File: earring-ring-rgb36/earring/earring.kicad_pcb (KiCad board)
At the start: 4 copper layers, 25 x 27.3 mm, 44 parts, among them J1 Conn_01x04, SW1 SW_Push, U2 STM32L031G6Ux

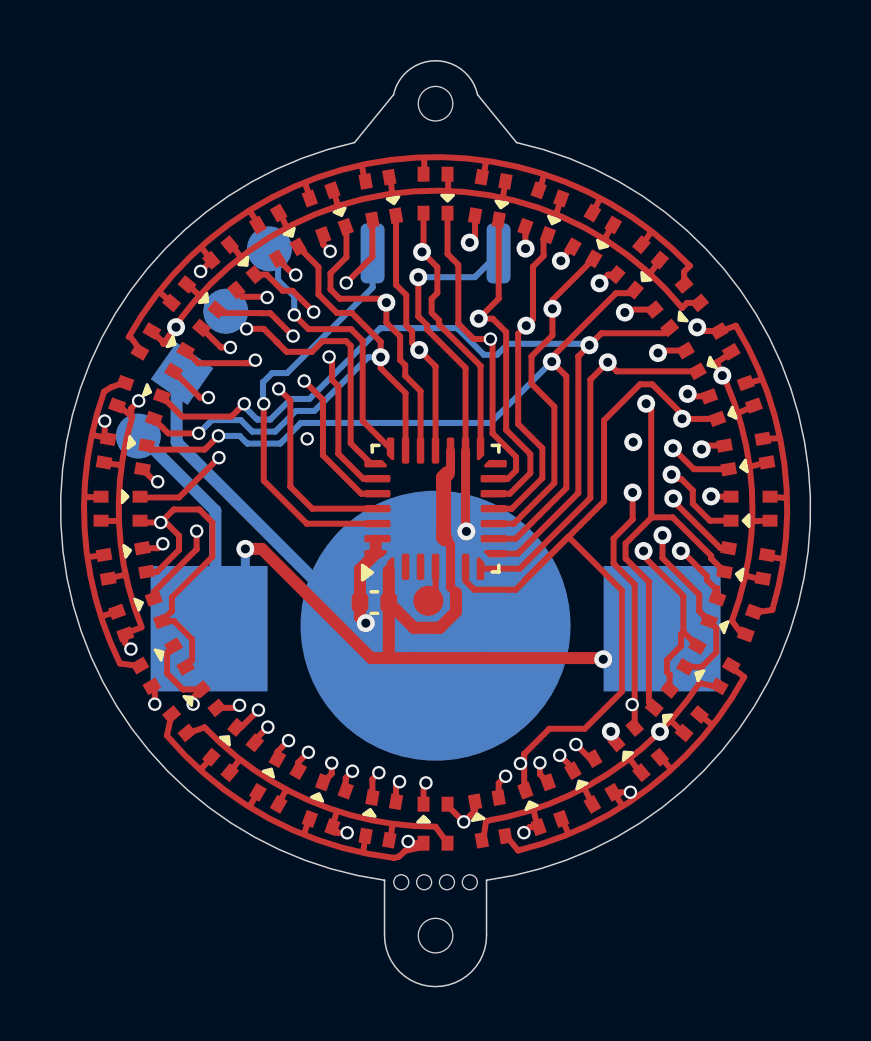
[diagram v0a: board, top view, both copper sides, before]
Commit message: earring-ring-rgb36: completely redid the schematic/PCB
Use 9x4 instead of 6x6 rows of LEDs. This should be more efficient to
control in software and actually simplifies the PCB a lot.

I also redid the routing of the PCB entirely:

  * Sit closer to the JLCPCB trace distance limit. Now most traces are
    0.2mm wide with 0.1mm spacing, whereas the limit is 0.10mm/0.10mm.
  * Put *two* traces between the LEDs. This simplifies the layout
    massively.
  * Switch to a two-layer board. We don't need the middle layers
    anymore with the above simplifications. This should make things
    cheaper and offer more options regarding color etc.
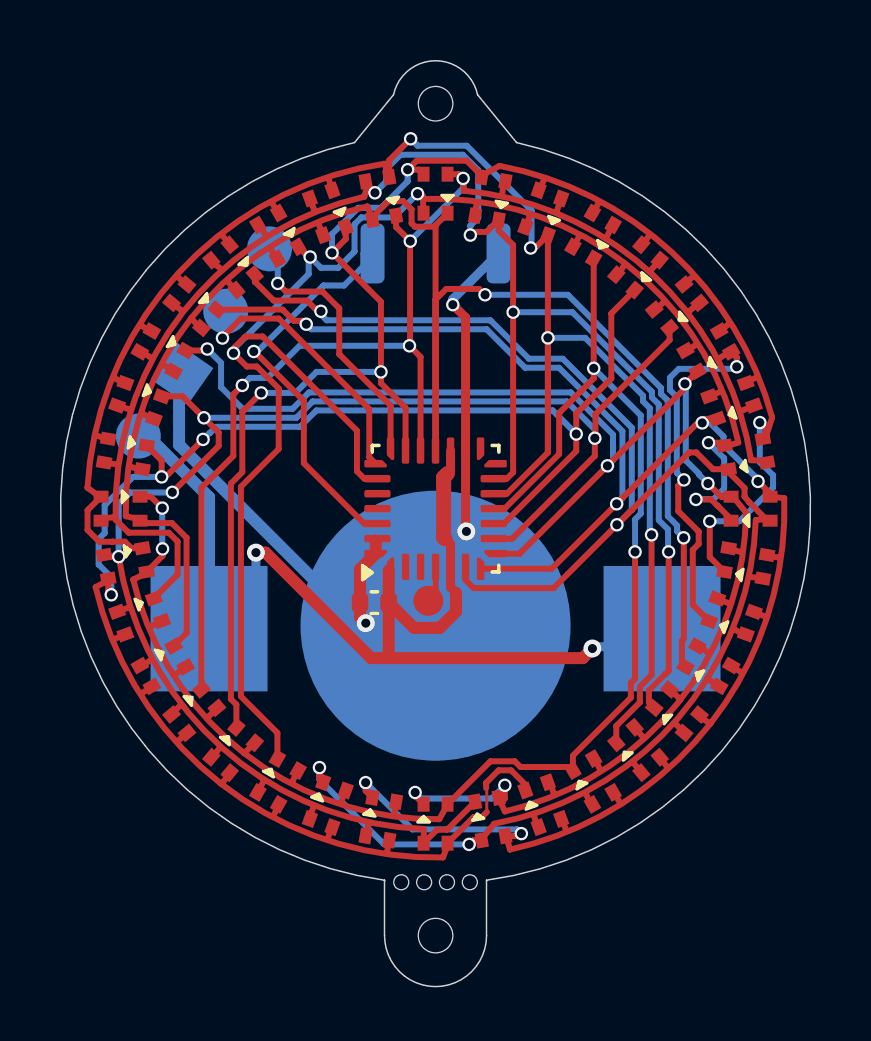
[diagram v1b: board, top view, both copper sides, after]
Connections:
- D1 pad 2: R1 -> A10
- D1 pad 3: G1 -> A11
- D1 pad 4: B1 -> A12
- D10 pad 2: A1 -> A7
- D10 pad 3: A2 -> A8
- D10 pad 4: A3 -> A9
- D11 pad 2: A1 -> A7
- D11 pad 3: A2 -> A8
- D11 pad 4: A3 -> A9
- D12 pad 2: A1 -> A7
- D12 pad 3: A2 -> A8
- D12 pad 4: A3 -> A9
- D13 pad 1: A12 -> A1
- D13 pad 2: A4 -> A7
- D13 pad 3: A5 -> A8
- D13 pad 4: A6 -> A9
- D14 pad 1: A11 -> A2
- D14 pad 2: A4 -> A7
- D14 pad 3: A5 -> A8
- D14 pad 4: A6 -> A9
- D15 pad 1: A10 -> A3
- D15 pad 2: A4 -> A7
- D15 pad 3: A5 -> A8
- D15 pad 4: A6 -> A9
- D16 pad 1: A9 -> A4
- D16 pad 2: A4 -> A7
- D16 pad 3: A5 -> A8
- D16 pad 4: A6 -> A9
- D17 pad 1: A8 -> A5
- D17 pad 2: A4 -> A7
- D17 pad 3: A5 -> A8
- D17 pad 4: A6 -> A9
- D18 pad 1: A7 -> A6
- D18 pad 2: A4 -> A7
- D18 pad 3: A5 -> A8
- D18 pad 4: A6 -> A9
- D19 pad 1: A6 -> A7
- D19 pad 2: A7 -> A4
- D19 pad 3: A8 -> A5
- D19 pad 4: A9 -> A6
- D2 pad 2: R1 -> A10
- D2 pad 3: G1 -> A11
- D2 pad 4: B1 -> A12
- D20 pad 1: A5 -> A8
- D20 pad 2: A7 -> A4
- D20 pad 3: A8 -> A5
- D20 pad 4: A9 -> A6
- D21 pad 1: A4 -> A9
- D21 pad 2: A7 -> A4
- D21 pad 3: A8 -> A5
- D21 pad 4: A9 -> A6
- D22 pad 1: A3 -> A10
- D22 pad 2: A7 -> A4
- D22 pad 3: A8 -> A5
- D22 pad 4: A9 -> A6
- D23 pad 1: A2 -> A11
- D23 pad 2: A7 -> A4
- D23 pad 3: A8 -> A5
- D23 pad 4: A9 -> A6
- D24 pad 1: A1 -> A12
- D24 pad 2: A7 -> A4
- D24 pad 3: A8 -> A5
- D24 pad 4: A9 -> A6
- D25 pad 2: A10 -> A4
- D25 pad 3: A11 -> A5
- D25 pad 4: A12 -> A6
- D26 pad 2: A10 -> A4
- D26 pad 3: A11 -> A5
- D26 pad 4: A12 -> A6
- D27 pad 2: A10 -> A4
- D27 pad 3: A11 -> A5
- D27 pad 4: A12 -> A6
- D28 pad 2: A10 -> A1
- D28 pad 3: A11 -> A2
- D28 pad 4: A12 -> A3
- D29 pad 2: A10 -> A1
- D29 pad 3: A11 -> A2
- D29 pad 4: A12 -> A3
- D3 pad 2: R1 -> A10
- D3 pad 3: G1 -> A11
- D3 pad 4: B1 -> A12
- D30 pad 2: A10 -> A1
- D30 pad 3: A11 -> A2
- D30 pad 4: A12 -> A3
- D31 pad 2: R1 -> A1
- D31 pad 3: G1 -> A2
- D31 pad 4: B1 -> A3
- D32 pad 2: R1 -> A1
- D32 pad 3: G1 -> A2
- D32 pad 4: B1 -> A3
- D33 pad 2: R1 -> A1
- D33 pad 3: G1 -> A2
- D33 pad 4: B1 -> A3
- D34 pad 2: R1 -> A1
- D34 pad 3: G1 -> A2
- D34 pad 4: B1 -> A3
- D35 pad 2: R1 -> A1
- D35 pad 3: G1 -> A2
- D35 pad 4: B1 -> A3
- D36 pad 2: R1 -> A1
- D36 pad 3: G1 -> A2
- D36 pad 4: B1 -> A3
- D4 pad 2: R1 -> A10
- D4 pad 3: G1 -> A11
- D4 pad 4: B1 -> A12
- D5 pad 2: R1 -> A10
- D5 pad 3: G1 -> A11
- D5 pad 4: B1 -> A12
- D6 pad 2: R1 -> A10
- D6 pad 3: G1 -> A11
- D6 pad 4: B1 -> A12
- D7 pad 2: A1 -> A10
- D7 pad 3: A2 -> A11
- D7 pad 4: A3 -> A12
- D8 pad 2: A1 -> A10
- D8 pad 3: A2 -> A11
- D8 pad 4: A3 -> A12
- D9 pad 2: A1 -> A10
- D9 pad 3: A2 -> A11
- D9 pad 4: A3 -> A12
- U2 pad 10: A4 -> A5
- U2 pad 11: A3 -> A4
- U2 pad 12: A2 -> A3
- U2 pad 13: A1 -> A2
- U2 pad 15: R1 -> unconnected-(U2-PB1-Pad15)
- U2 pad 18: A12 -> A1
- U2 pad 19: A11 -> A12
- U2 pad 20: A10 -> A11
- U2 pad 23: A9 -> A10
- U2 pad 24: G1 -> unconnected-(U2-PB3-Pad24)
- U2 pad 25: B1 -> unconnected-(U2-PB6-Pad25)
- U2 pad 6: A8 -> A9
- U2 pad 7: A7 -> A8
- U2 pad 8: A6 -> A7
- U2 pad 9: A5 -> A6
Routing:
- net R1: track 40.4 -> 0.00 mm, vias 12 -> 0
- net A4: track 70.1 -> 33.1 mm, vias 9 -> 4
- net A10: track 55.3 -> 38.5 mm, vias 6 -> 5
- net A5: track 52.4 -> 36.9 mm
- net A7: track 51.2 -> 35.8 mm, vias 8 -> 6
- net A1: track 55.7 -> 40.5 mm, vias 8 -> 2
- net A8: track 52.7 -> 38.3 mm, vias 4 -> 6
- net G1: track 13.0 -> 0.00 mm, vias 2 -> 0
- net B1: track 12.5 -> 0.00 mm, vias 2 -> 0
- net A6: track 47.5 -> 35.3 mm, vias 5 -> 4
- net A9: track 49.6 -> 39.4 mm, vias 5 -> 4
- net A11: track 48.8 -> 39.6 mm, vias 5 -> 6
- net A2: track 44.1 -> 39.3 mm
- net A3: track 46.4 -> 41.6 mm, vias 5 -> 4
- net GND: track 28.8 -> 26.7 mm
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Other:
- copper layers 4 -> 2

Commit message: earring-ring-rgb36: rotate net names so the labels make a bit more sense
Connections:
- D1 pad 1: A1 -> A4
- D1 pad 2: A10 -> A1
- D1 pad 3: A11 -> A2
- D1 pad 4: A12 -> A3
- D10 pad 1: A10 -> A1
- D10 pad 2: A7 -> A10
- D10 pad 3: A8 -> A11
- D10 pad 4: A9 -> A12
- D11 pad 1: A11 -> A2
- D11 pad 2: A7 -> A10
- D11 pad 3: A8 -> A11
- D11 pad 4: A9 -> A12
- D12 pad 1: A12 -> A3
- D12 pad 2: A7 -> A10
- D12 pad 3: A8 -> A11
- D12 pad 4: A9 -> A12
- D13 pad 1: A1 -> A4
- D13 pad 2: A7 -> A10
- D13 pad 3: A8 -> A11
- D13 pad 4: A9 -> A12
- D14 pad 1: A2 -> A5
- D14 pad 2: A7 -> A10
- D14 pad 3: A8 -> A11
- D14 pad 4: A9 -> A12
- D15 pad 1: A3 -> A6
- D15 pad 2: A7 -> A10
- D15 pad 3: A8 -> A11
- D15 pad 4: A9 -> A12
- D16 pad 1: A4 -> A7
- D16 pad 2: A7 -> A10
- D16 pad 3: A8 -> A11
- D16 pad 4: A9 -> A12
- D17 pad 1: A5 -> A8
- D17 pad 2: A7 -> A10
- D17 pad 3: A8 -> A11
- D17 pad 4: A9 -> A12
- D18 pad 1: A6 -> A9
- D18 pad 2: A7 -> A10
- D18 pad 3: A8 -> A11
- D18 pad 4: A9 -> A12
- D19 pad 1: A7 -> A10
- D19 pad 2: A4 -> A7
- D19 pad 3: A5 -> A8
- D19 pad 4: A6 -> A9
- D2 pad 1: A2 -> A5
- D2 pad 2: A10 -> A1
- D2 pad 3: A11 -> A2
- D2 pad 4: A12 -> A3
- D20 pad 1: A8 -> A11
- D20 pad 2: A4 -> A7
- D20 pad 3: A5 -> A8
- D20 pad 4: A6 -> A9
- D21 pad 1: A9 -> A12
- D21 pad 2: A4 -> A7
- D21 pad 3: A5 -> A8
- D21 pad 4: A6 -> A9
- D22 pad 1: A10 -> A1
- D22 pad 2: A4 -> A7
- D22 pad 3: A5 -> A8
- D22 pad 4: A6 -> A9
- D23 pad 1: A11 -> A2
- D23 pad 2: A4 -> A7
- D23 pad 3: A5 -> A8
- D23 pad 4: A6 -> A9
- D24 pad 1: A12 -> A3
- D24 pad 2: A4 -> A7
- D24 pad 3: A5 -> A8
- D24 pad 4: A6 -> A9
- D25 pad 1: A1 -> A4
- D25 pad 2: A4 -> A7
- D25 pad 3: A5 -> A8
- D25 pad 4: A6 -> A9
- D26 pad 1: A2 -> A5
- D26 pad 2: A4 -> A7
- D26 pad 3: A5 -> A8
- D26 pad 4: A6 -> A9
- D27 pad 1: A3 -> A6
- D27 pad 2: A4 -> A7
- D27 pad 3: A5 -> A8
- D27 pad 4: A6 -> A9
- D28 pad 1: A4 -> A7
- D28 pad 2: A1 -> A4
- D28 pad 3: A2 -> A5
- D28 pad 4: A3 -> A6
- D29 pad 1: A5 -> A8
- D29 pad 2: A1 -> A4
- D29 pad 3: A2 -> A5
- D29 pad 4: A3 -> A6
- D3 pad 1: A3 -> A6
- D3 pad 2: A10 -> A1
- D3 pad 3: A11 -> A2
- D3 pad 4: A12 -> A3
- D30 pad 1: A6 -> A9
- D30 pad 2: A1 -> A4
- D30 pad 3: A2 -> A5
- D30 pad 4: A3 -> A6
- D31 pad 1: A7 -> A10
- D31 pad 2: A1 -> A4
- D31 pad 3: A2 -> A5
- D31 pad 4: A3 -> A6
- D32 pad 1: A8 -> A11
- D32 pad 2: A1 -> A4
- D32 pad 3: A2 -> A5
- D32 pad 4: A3 -> A6
- D33 pad 1: A9 -> A12
- D33 pad 2: A1 -> A4
- D33 pad 3: A2 -> A5
- D33 pad 4: A3 -> A6
- D34 pad 1: A10 -> A1
- D34 pad 2: A1 -> A4
- D34 pad 3: A2 -> A5
- D34 pad 4: A3 -> A6
- D35 pad 1: A11 -> A2
- D35 pad 2: A1 -> A4
- D35 pad 3: A2 -> A5
- D35 pad 4: A3 -> A6
- D36 pad 1: A12 -> A3
- D36 pad 2: A1 -> A4
- D36 pad 3: A2 -> A5
- D36 pad 4: A3 -> A6
- D4 pad 1: A4 -> A7
- D4 pad 2: A10 -> A1
- D4 pad 3: A11 -> A2
- D4 pad 4: A12 -> A3
- D5 pad 1: A5 -> A8
- D5 pad 2: A10 -> A1
- D5 pad 3: A11 -> A2
- D5 pad 4: A12 -> A3
- D6 pad 1: A6 -> A9
- D6 pad 2: A10 -> A1
- D6 pad 3: A11 -> A2
- D6 pad 4: A12 -> A3
- D7 pad 1: A7 -> A10
- D7 pad 2: A10 -> A1
- D7 pad 3: A11 -> A2
- D7 pad 4: A12 -> A3
- D8 pad 1: A8 -> A11
- D8 pad 2: A10 -> A1
- D8 pad 3: A11 -> A2
- D8 pad 4: A12 -> A3
- D9 pad 1: A9 -> A12
- D9 pad 2: A10 -> A1
- D9 pad 3: A11 -> A2
- D9 pad 4: A12 -> A3
- U2 pad 10: A5 -> A8
- U2 pad 11: A4 -> A7
- U2 pad 12: A3 -> A6
- U2 pad 13: A2 -> A5
- U2 pad 18: A1 -> A4
- U2 pad 19: A12 -> A3
- U2 pad 20: A11 -> A2
- U2 pad 23: A10 -> A1
- U2 pad 6: A9 -> A12
- U2 pad 7: A8 -> A11
- U2 pad 8: A7 -> A10
- U2 pad 9: A6 -> A9
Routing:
- net A4: track 33.1 -> 40.5 mm, vias 4 -> 2
- net A6: track 35.3 -> 41.6 mm
- net A9: track 39.4 -> 35.3 mm
- net A7: track 35.8 -> 33.1 mm, vias 6 -> 4
- net A10: track 38.5 -> 35.8 mm, vias 5 -> 6
- net A5: track 36.9 -> 39.3 mm
- net A1: track 40.5 -> 38.5 mm, vias 2 -> 5
- net A11: track 39.6 -> 38.3 mm
- net A8: track 38.3 -> 36.9 mm, vias 6 -> 4
- net A3: track 41.6 -> 40.3 mm, vias 4 -> 6
- net A12: track 40.3 -> 39.4 mm, vias 6 -> 4
- net A2: track 39.3 -> 39.6 mm, vias 4 -> 6

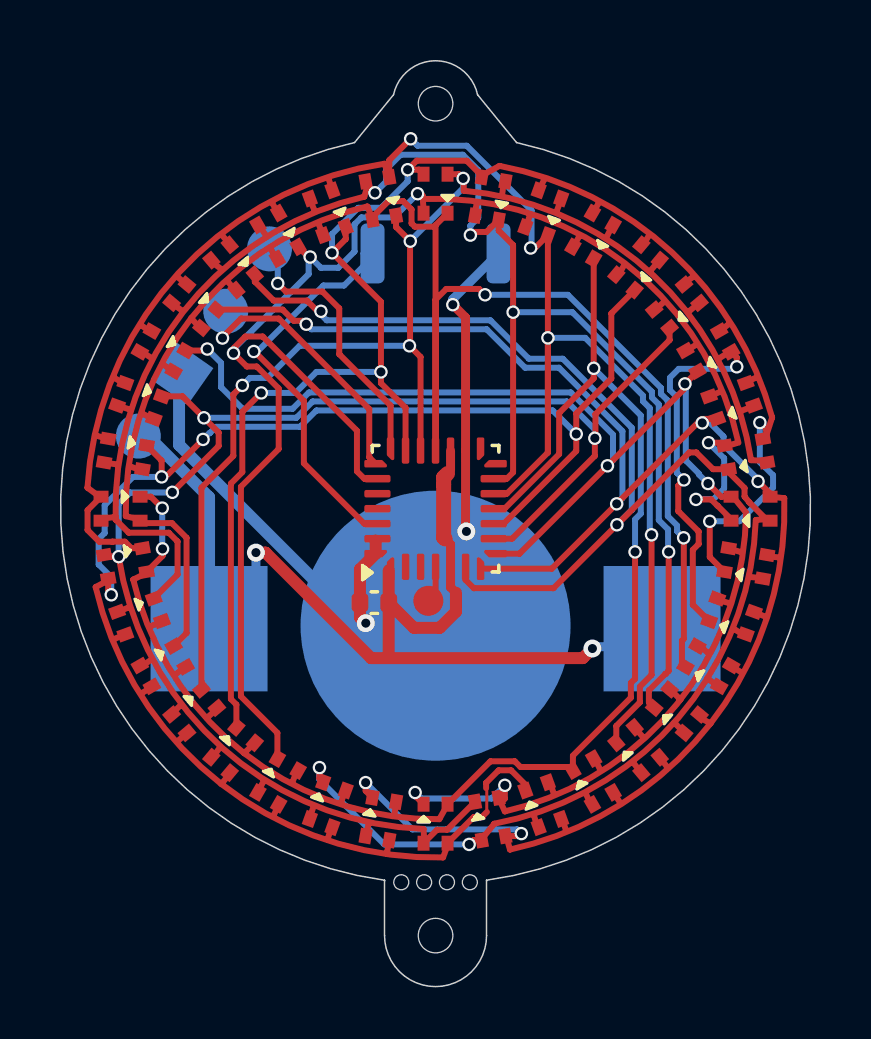
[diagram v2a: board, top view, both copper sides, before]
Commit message: earring-ring-rgb36: updated PCB in many ways
 - updated to KiCad 9
 - added resistors for the LEDs (now assuming individual charlieplexing)
 - added MOSFET for reverse current protection
 - redid most of the wiring on the PCB, with the addition of the
   resistors
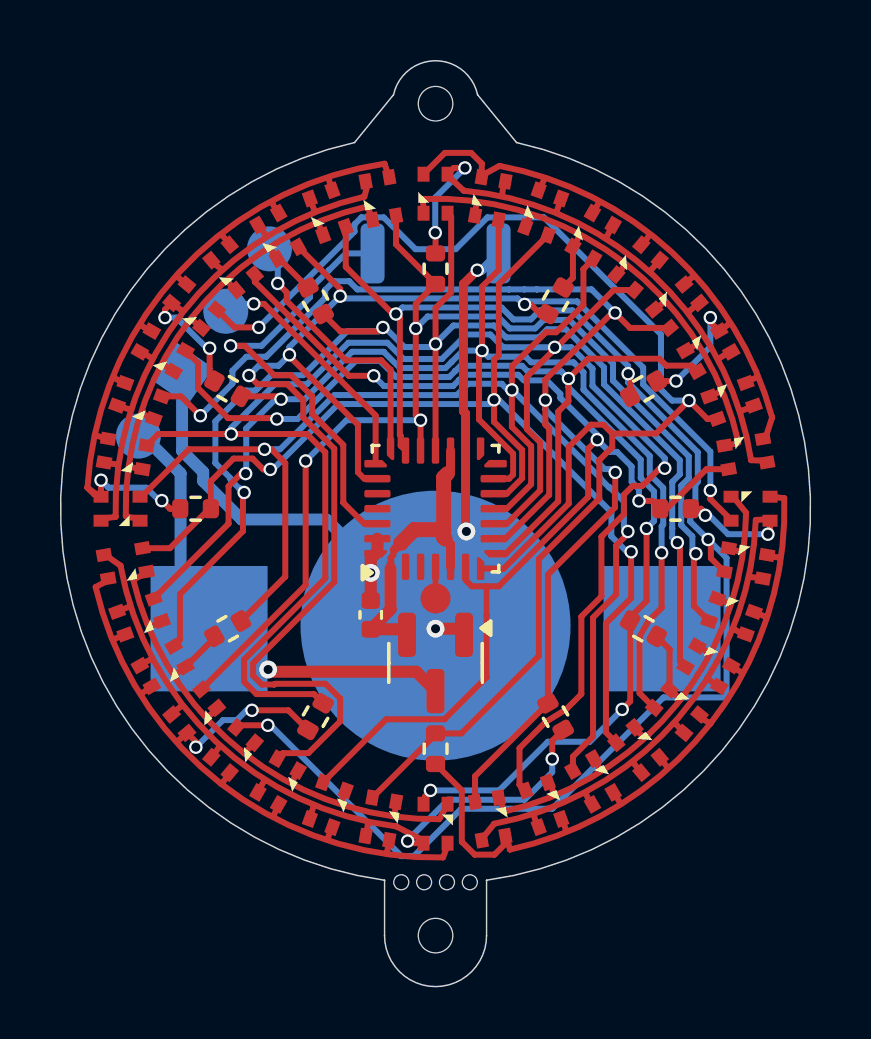
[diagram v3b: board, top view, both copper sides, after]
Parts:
- added Q1: AO3401A, Package_TO_SOT_SMD:SOT-23, F.Cu at (0.00, 5.14)
- added R1: 1k, Resistor_SMD:R_0402_1005Metric, F.Cu at (4.00, -6.93)
- added R10: 1k, Resistor_SMD:R_0402_1005Metric, F.Cu at (6.93, 4.00)
- added R11: 1k, Resistor_SMD:R_0402_1005Metric, F.Cu at (0.00, 8.00)
- added R12: 220, Resistor_SMD:R_0402_1005Metric, F.Cu at (8.00, 0.00)
- added R2: 1k, Resistor_SMD:R_0402_1005Metric, F.Cu at (6.93, -4.00)
- added R3: 220, Resistor_SMD:R_0402_1005Metric, F.Cu at (0.00, -8.00)
- added R4: 1k, Resistor_SMD:R_0402_1005Metric, F.Cu at (-4.00, -6.93)
- added R5: 1k, Resistor_SMD:R_0402_1005Metric, F.Cu at (-6.93, -4.00)
- added R6: 220, Resistor_SMD:R_0402_1005Metric, F.Cu at (-8.00, 0.00)
- added R7: 1k, Resistor_SMD:R_0402_1005Metric, F.Cu at (-6.93, 4.00)
- added R8: 1k, Resistor_SMD:R_0402_1005Metric, F.Cu at (-4.00, 6.93)
- added R9: 220, Resistor_SMD:R_0402_1005Metric, F.Cu at (4.00, 6.93)
- moved C2 0.43 mm to (-2.16, 3.54), turned to 90 degrees
- moved TP1 0.25 mm to (0.00, 2.99)
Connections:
- BT1 pad 1: VCC -> VBAT
- D1 pad 2: A1 -> A1R
- D1 pad 3: A2 -> A2R
- D1 pad 4: A3 -> A3R
- D10 pad 2: A10 -> A10R
- D10 pad 3: A11 -> A11R
- D10 pad 4: A12 -> A12R
- D11 pad 2: A10 -> A10R
- D11 pad 3: A11 -> A11R
- D11 pad 4: A12 -> A12R
- D12 pad 2: A10 -> A10R
- D12 pad 3: A11 -> A11R
- D12 pad 4: A12 -> A12R
- D13 pad 2: A10 -> A10R
- D13 pad 3: A11 -> A11R
- D13 pad 4: A12 -> A12R
- D14 pad 2: A10 -> A10R
- D14 pad 3: A11 -> A11R
- D14 pad 4: A12 -> A12R
- D15 pad 2: A10 -> A10R
- D15 pad 3: A11 -> A11R
- D15 pad 4: A12 -> A12R
- D16 pad 2: A10 -> A10R
- D16 pad 3: A11 -> A11R
- D16 pad 4: A12 -> A12R
- D17 pad 2: A10 -> A10R
- D17 pad 3: A11 -> A11R
- D17 pad 4: A12 -> A12R
- D18 pad 2: A10 -> A10R
- D18 pad 3: A11 -> A11R
- D18 pad 4: A12 -> A12R
- D19 pad 2: A7 -> A7R
- D19 pad 3: A8 -> A8R
- D19 pad 4: A9 -> A9R
- D2 pad 2: A1 -> A1R
- D2 pad 3: A2 -> A2R
- D2 pad 4: A3 -> A3R
- D20 pad 2: A7 -> A7R
- D20 pad 3: A8 -> A8R
- D20 pad 4: A9 -> A9R
- D21 pad 2: A7 -> A7R
- D21 pad 3: A8 -> A8R
- D21 pad 4: A9 -> A9R
- D22 pad 2: A7 -> A7R
- D22 pad 3: A8 -> A8R
- D22 pad 4: A9 -> A9R
- D23 pad 2: A7 -> A7R
- D23 pad 3: A8 -> A8R
- D23 pad 4: A9 -> A9R
- D24 pad 2: A7 -> A7R
- D24 pad 3: A8 -> A8R
- D24 pad 4: A9 -> A9R
- D25 pad 2: A7 -> A7R
- D25 pad 3: A8 -> A8R
- D25 pad 4: A9 -> A9R
- D26 pad 2: A7 -> A7R
- D26 pad 3: A8 -> A8R
- D26 pad 4: A9 -> A9R
- D27 pad 2: A7 -> A7R
- D27 pad 3: A8 -> A8R
- D27 pad 4: A9 -> A9R
- D28 pad 2: A4 -> A4R
- D28 pad 3: A5 -> A5R
- D28 pad 4: A6 -> A6R
- D29 pad 2: A4 -> A4R
- D29 pad 3: A5 -> A5R
- D29 pad 4: A6 -> A6R
- D3 pad 2: A1 -> A1R
- D3 pad 3: A2 -> A2R
- D3 pad 4: A3 -> A3R
- D30 pad 2: A4 -> A4R
- D30 pad 3: A5 -> A5R
- D30 pad 4: A6 -> A6R
- D31 pad 2: A4 -> A4R
- D31 pad 3: A5 -> A5R
- D31 pad 4: A6 -> A6R
- D32 pad 2: A4 -> A4R
- D32 pad 3: A5 -> A5R
- D32 pad 4: A6 -> A6R
- D33 pad 2: A4 -> A4R
- D33 pad 3: A5 -> A5R
- D33 pad 4: A6 -> A6R
- D34 pad 2: A4 -> A4R
- D34 pad 3: A5 -> A5R
- D34 pad 4: A6 -> A6R
- D35 pad 2: A4 -> A4R
- D35 pad 3: A5 -> A5R
- D35 pad 4: A6 -> A6R
- D36 pad 2: A4 -> A4R
- D36 pad 3: A5 -> A5R
- D36 pad 4: A6 -> A6R
- D4 pad 2: A1 -> A1R
- D4 pad 3: A2 -> A2R
- D4 pad 4: A3 -> A3R
- D5 pad 2: A1 -> A1R
- D5 pad 3: A2 -> A2R
- D5 pad 4: A3 -> A3R
- D6 pad 2: A1 -> A1R
- D6 pad 3: A2 -> A2R
- D6 pad 4: A3 -> A3R
- D7 pad 2: A1 -> A1R
- D7 pad 3: A2 -> A2R
- D7 pad 4: A3 -> A3R
- D8 pad 2: A1 -> A1R
- D8 pad 3: A2 -> A2R
- D8 pad 4: A3 -> A3R
- D9 pad 2: A1 -> A1R
- D9 pad 3: A2 -> A2R
- D9 pad 4: A3 -> A3R
- J1 pad 1: VCC -> VBAT
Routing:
- net VCC: track 37.9 -> 10.2 mm, vias 2 -> 0
- net A8: track 36.9 -> 60.1 mm, vias 4 -> 3
- net VBAT: track 0.00 -> 15.7 mm, vias 0 -> 1
- net A7: track 33.1 -> 46.7 mm, vias 4 -> 3
- net A2: track 39.6 -> 52.3 mm, vias 6 -> 4
- net A10: track 35.8 -> 48.1 mm, vias 6 -> 5
- net A11: track 38.3 -> 49.9 mm, vias 6 -> 2
- net A1: track 38.5 -> 50.0 mm
- net A9: track 35.3 -> 46.1 mm
- net A9R: track 0.00 -> 7.91 mm, vias 0 -> 2
- net A2R: track 0.00 -> 6.64 mm, vias 0 -> 2
- net A4: track 40.5 -> 46.3 mm, vias 2 -> 4
- net A8R: track 0.00 -> 5.11 mm, vias 0 -> 2
- net A11R: track 0.00 -> 4.99 mm
- net A5: track 39.3 -> 43.6 mm
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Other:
- board text added: "LED earring v0.3"
- board text removed: "LED earring v0.2"
